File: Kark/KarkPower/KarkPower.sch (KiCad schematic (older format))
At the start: 35 parts, among them J101 CAN_1, J102 CAN_2, J103 CAN_3, J104 CAN_4, J105 CAN_5, J106 CAN_6, J107 CAN_7, J108 CAN_8, J109 CAN_9, J110 JPR_1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

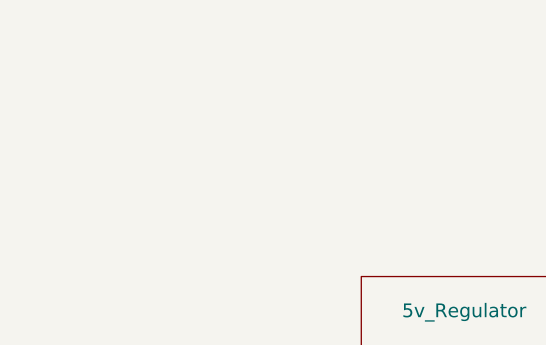
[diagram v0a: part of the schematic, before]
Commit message: PCB Developed Further
Organized and optimized part layout.
(wires not started)
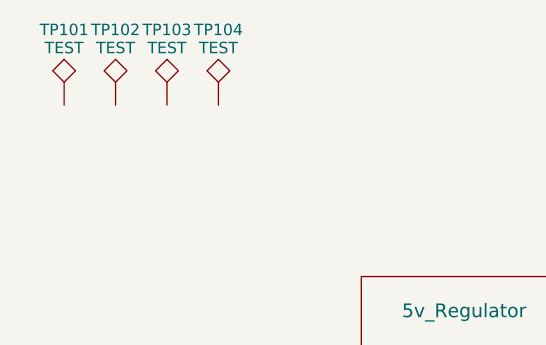
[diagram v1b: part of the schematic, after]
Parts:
- added TP101, TP102, TP103, TP104: TEST, Mounting_Holes:MountingHole_3.2mm_M3_Pad, symbol TEST
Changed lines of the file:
@@
 Wire Wire Line
 	5625 3700 5625 3075
+$Comp
+L TEST TP101
+U 1 1 5A635A3C
+P 1075 2000
+F 0 "TP101" H 1075 2300 50  0000 C BNN
+F 1 "TEST" H 1075 2250 50  0000 C CNN
+F 2 "Mounting_Holes:MountingHole_3.2mm_M3_Pad" H 1075 2000 50  0001 C CNN
+F 3 "" H 1075 2000 50  0001 C CNN
+	1    1075 2000
+	1    0    0    -1
+$EndComp
+$Comp
+L TEST TP102
+U 1 1 5A635CC5
+P 1300 2000
+F 0 "TP102" H 1300 2300 50  0000 C BNN
+F 1 "TEST" H 1300 2250 50  0000 C CNN
+F 2 "Mounting_Holes:MountingHole_3.2mm_M3_Pad" H 1300 2000 50  0001 C CNN
+F 3 "" H 1300 2000 50  0001 C CNN
+	1    1300 2000
+	1    0    0    -1
+$EndComp
+$Comp
+L TEST TP103
+U 1 1 5A635D55
+P 1525 2000
+F 0 "TP103" H 1525 2300 50  0000 C BNN
+F 1 "TEST" H 1525 2250 50  0000 C CNN
+F 2 "Mounting_Holes:MountingHole_3.2mm_M3_Pad" H 1525 2000 50  0001 C CNN
+F 3 "" H 1525 2000 50  0001 C CNN
+	1    1525 2000
+	1    0    0    -1
+$EndComp
+$Comp
+L TEST TP104
+U 1 1 5A635DDC
+P 1750 2000
+F 0 "TP104" H 1750 2300 50  0000 C BNN
+F 1 "TEST" H 1750 2250 50  0000 C CNN
+F 2 "Mounting_Holes:MountingHole_3.2mm_M3_Pad" H 1750 2000 50  0001 C CNN
+F 3 "" H 1750 2000 50  0001 C CNN
+	1    1750 2000
+	1    0    0    -1
+$EndComp
 $EndSCHEMATC

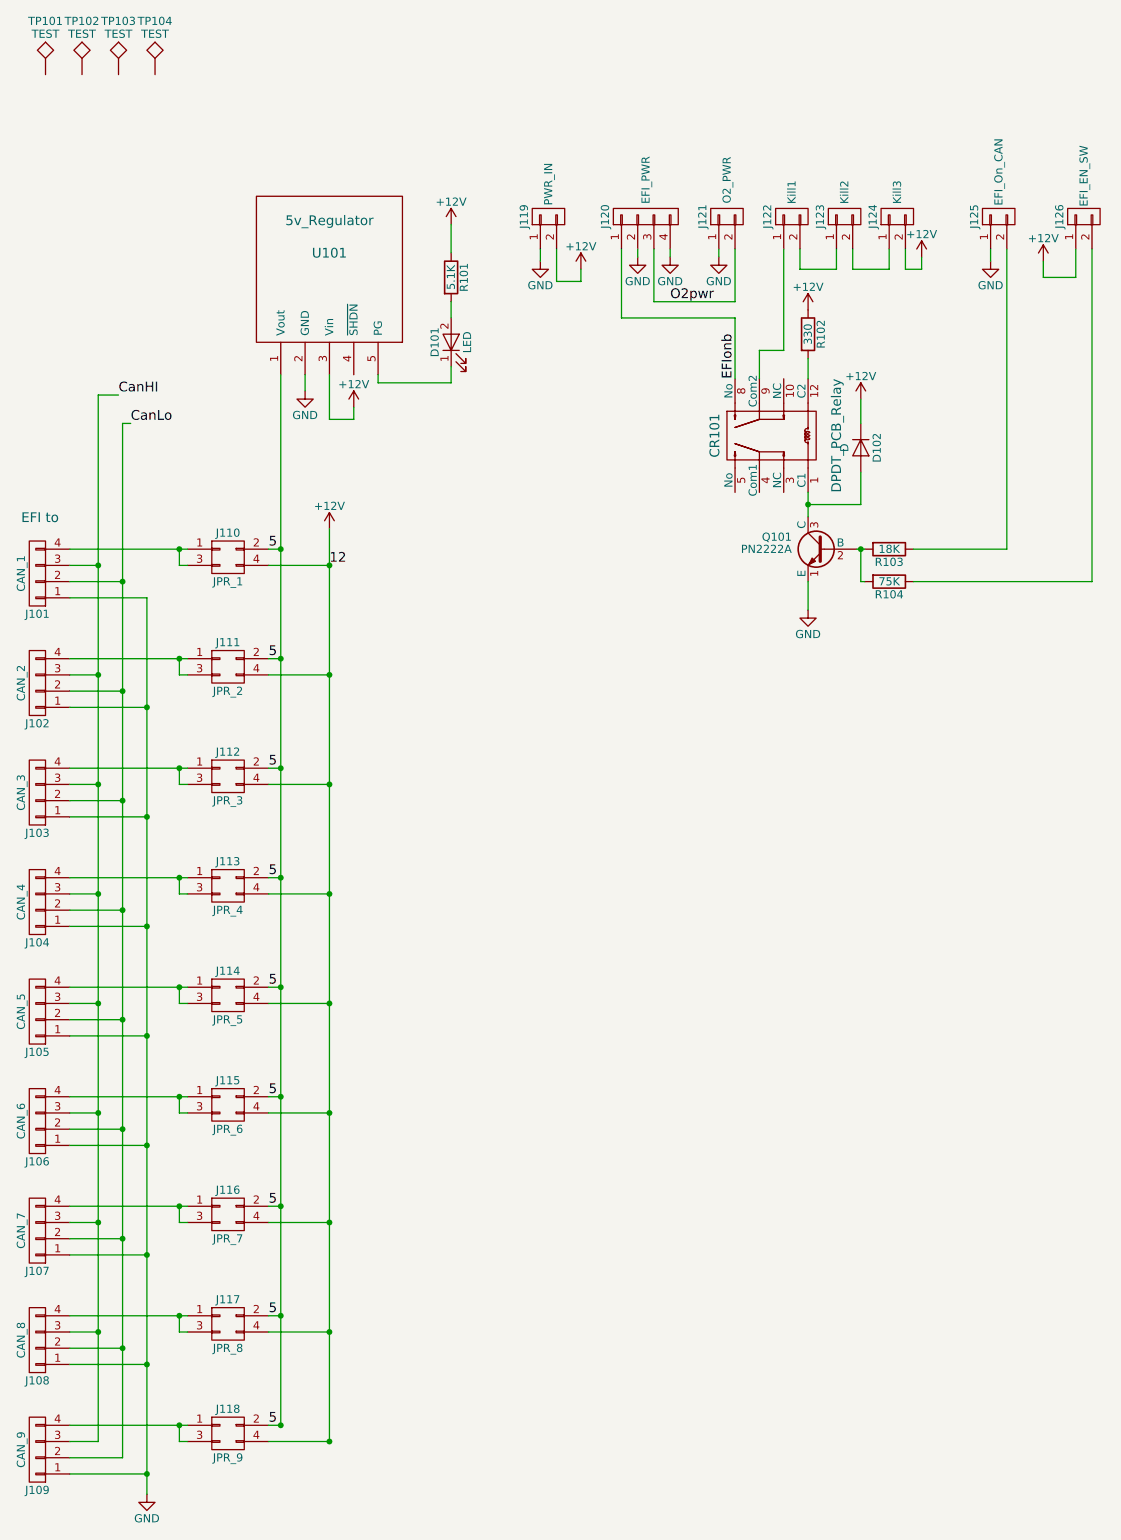
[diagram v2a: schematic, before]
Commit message: Added Starter and Fuel pump
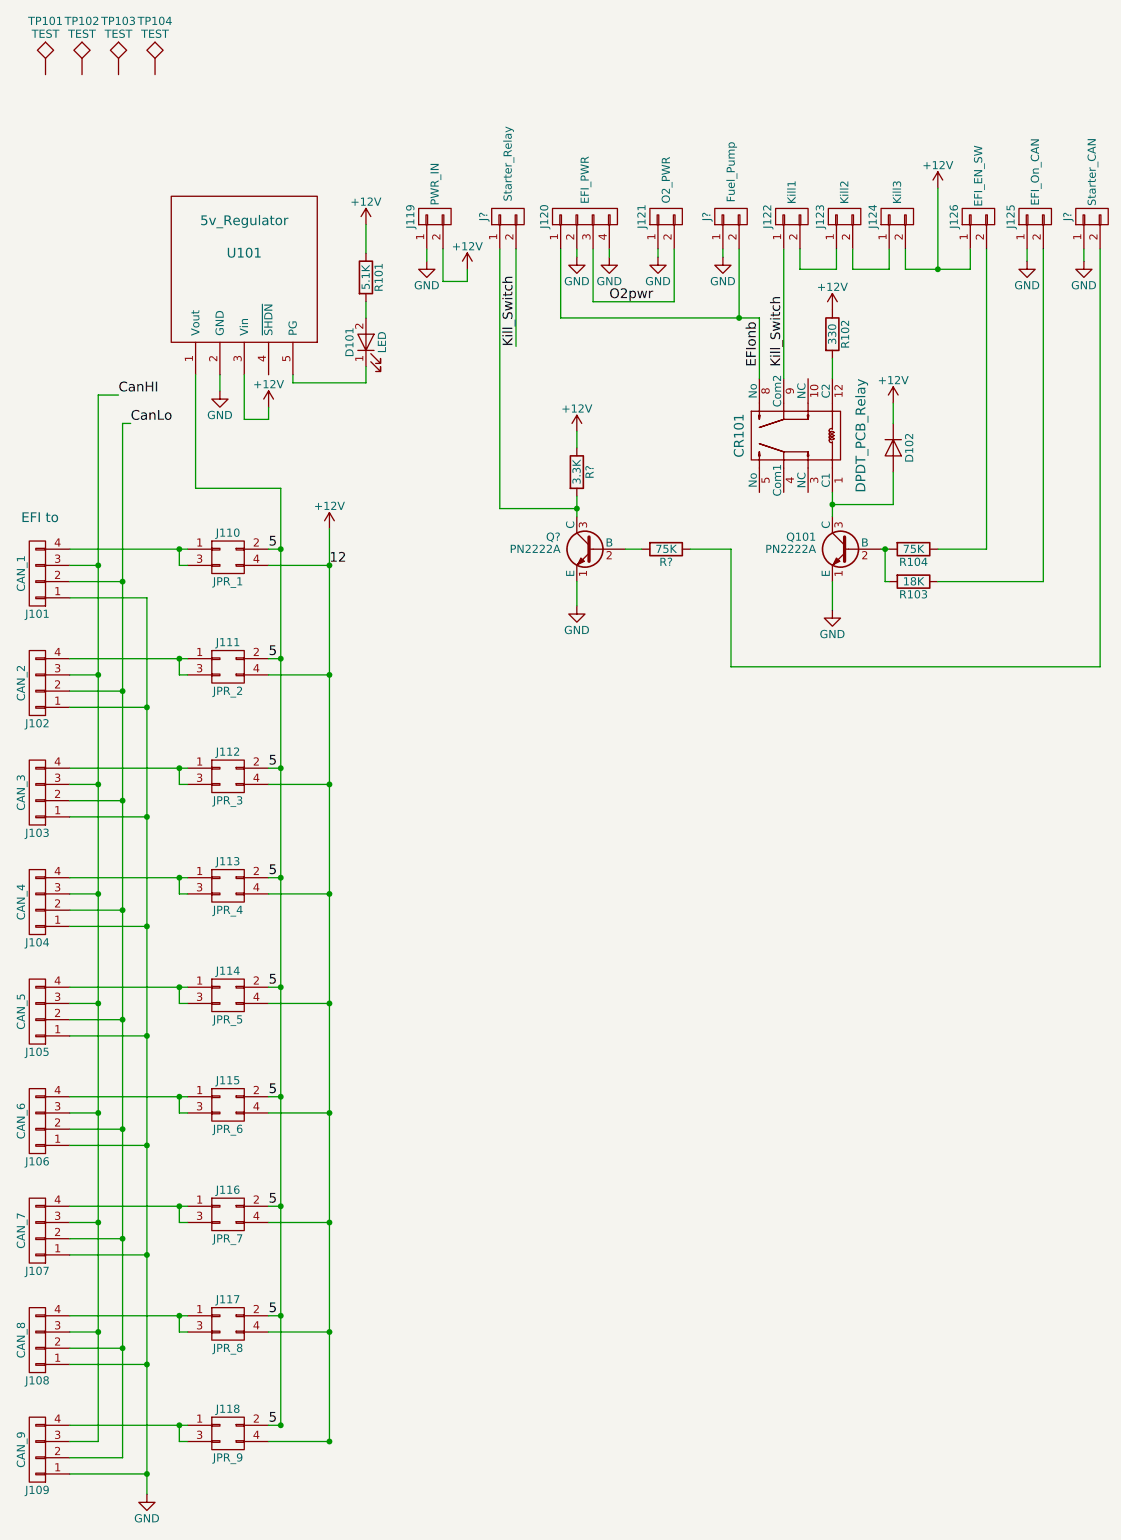
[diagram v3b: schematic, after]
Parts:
- added J?: Fuel_Pump, supermileage_footprints:Molex-UltraFit-2p, symbol CONN_01X02
- added J?: Starter_CAN, supermileage_footprints:Molex-UltraFit-2p, symbol CONN_01X02
- added J?: Starter_Relay, supermileage_footprints:Molex-UltraFit-2p, symbol CONN_01X02
- added Q?: PN2222A, TO_SOT_Packages_THT:TO-92_Inline_Wide, symbol PN2222A
- added R?: 3.3K, symbol R
- added R?: 75K, Resistors_THT:R_Axial_DIN0207_L6.3mm_D2.5mm_P7.62mm_Horizontal, symbol R
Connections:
- net +12V: now also R?.1
- net EFIonb: now also J?.2 (P2)
- net GND: now also J?.1 (P1), J?.1 (P1), Q?.1 (E)
- net Kill_Switch: now reaches CR101.9 (Com2), J122.1 (P1)
- net Kill_Switch: now also J?.2 (P2)
- new net: Q?.2 (B), R?.2
- new net: J?.1 (P1), Q?.3 (C), R?.2
- new net: J?.2 (P2), R?.1
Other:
- moved on the sheet: CR101, D101, D102, J119, J120, J121, J125, J126, Q101, R101, R102, R103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

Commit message: Created can breakout
Added can boards fro sensors and integrated the computer to the can system.
Created the Can powering system.
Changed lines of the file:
@@
 LIBS:supermileage_computers
 LIBS:supermileage_sensors
+LIBS:EllicottDisplay
+LIBS:EllicottInterface
+LIBS:EllicottMicrocontrollers
+LIBS:EllicottMisc
+LIBS:EllicottPower
 LIBS:KarkSchematics-cache
 EELAYER 25 0
@@
 $Descr A4 8268 11693 portrait
 encoding utf-8
-Sheet 4 6
+Sheet 3 9
 Title "Karch Main Power Distribution Hub"
 Date "01/13/18"
@@
 Kill_Switch
 Wire Wire Line
-	1400 3975 1400 5025
-Wire Wire Line
-	1400 5025 1400 5700
-Wire Wire Line
-	1400 5700 1400 6375
-Wire Wire Line
-	1400 6375 1400 7050
-Wire Wire Line
-	1400 7050 1400 7725
-Wire Wire Line
-	1400 7725 1400 8400
-Wire Wire Line
-	1400 8400 1400 9075
-Wire Wire Line
-	1400 9075 1400 9750
-Wire Wire Line
-	1400 9750 1400 10425
-Wire Wire Line
-	1550 4150 1550 5125
-Wire Wire Line
-	1550 5125 1550 5800
-Wire Wire Line
-	1550 5800 1550 6475
-Wire Wire Line
-	1550 6475 1550 7150
-Wire Wire Line
-	1550 7150 1550 7825
-Wire Wire Line
-	1550 7825 1550 8500
-Wire Wire Line
-	1550 8500 1550 9175
-Wire Wire Line
-	1550 9175 1550 9850
-Wire Wire Line
-	1550 9850 1550 10525
+	1400 3975 1400 10425
+Wire Wire Line
+	1550 4150 1550 10525
 Wire Wire Line
 	5725 3075 5725 3200
@@
 	6275 3200 6275 3075
 Wire Wire Line
-	2525 4550 2525 4925
-Wire Wire Line
-	2525 4925 2525 5600
-Wire Wire Line
-	2525 5600 2525 6275
-Wire Wire Line
-	2525 6275 2525 6950
-Wire Wire Line
-	2525 6950 2525 7625
-Wire Wire Line
-	2525 7625 2525 8300
-Wire Wire Line
-	2525 8300 2525 8975
-Wire Wire Line
-	2525 8975 2525 9650
-Wire Wire Line
-	2525 9650 2525 10325
+	2525 4550 2525 10325
 Connection ~ 2525 4925
 Connection ~ 2825 5025
 Wire Wire Line
-	1700 5225 1700 5900
-Wire Wire Line
-	1700 5900 1700 6575
-Wire Wire Line
-	1700 6575 1700 7250
-Wire Wire Line
-	1700 7250 1700 7925
-Wire Wire Line
-	1700 7925 1700 8600
-Wire Wire Line
-	1700 8600 1700 9275
-Wire Wire Line
-	1700 9275 1700 9950
-Wire Wire Line
-	1700 9950 1700 10625
-Wire Wire Line
-	1700 10625 1700 10750
+	1700 5225 1700 10750
 Wire Wire Line
 	1550 4150 1600 4150
@@
 Connection ~ 1400 5025
 Wire Wire Line
-	1225 5600 1900 5600
-Wire Wire Line
-	1900 5600 1950 5600
+	1225 5600 1950 5600
 Wire Wire Line
 	1700 5900 1225 5900
@@
 Connection ~ 2825 5700
 Wire Wire Line
-	1225 4925 1900 4925
-Wire Wire Line
-	1900 4925 1950 4925
+	1225 4925 1950 4925
 Wire Wire Line
 	2525 4925 2450 4925
@@
 Connection ~ 1900 4925
 Wire Wire Line
-	1225 6275 1900 6275
-Wire Wire Line
-	1900 6275 1950 6275
+	1225 6275 1950 6275
 Wire Wire Line
 	1700 6575 1225 6575
@@
 Connection ~ 2825 6375
 Wire Wire Line
-	1225 6950 1900 6950
-Wire Wire Line
-	1900 6950 1950 6950
+	1225 6950 1950 6950
 Wire Wire Line
 	1700 7250 1225 7250
@@
 Connection ~ 2825 7050
 Wire Wire Line
-	1225 7625 1900 7625
-Wire Wire Line
-	1900 7625 1950 7625
+	1225 7625 1950 7625
 Wire Wire Line
 	1700 7925 1225 7925
@@
 Connection ~ 2525 7625
 Wire Wire Line
-	1225 8300 1900 8300
-Wire Wire Line
-	1900 8300 1950 8300
+	1225 8300 1950 8300
 Wire Wire Line
 	1700 8600 1225 8600
@@
 Connection ~ 2825 8400
 Wire Wire Line
-	1225 8975 1900 8975
-Wire Wire Line
-	1900 8975 1950 8975
+	1225 8975 1950 8975
 Wire Wire Line
 	1700 9275 1225 9275
@@
 Connection ~ 2825 9075
 Wire Wire Line
-	1225 9650 1900 9650
-Wire Wire Line
-	1900 9650 1950 9650
+	1225 9650 1950 9650
 Wire Wire Line
 	1700 9950 1225 9950
@@
 Connection ~ 2825 9750
 Wire Wire Line
-	1225 10325 1900 10325
-Wire Wire Line
-	1900 10325 1950 10325
+	1225 10325 1950 10325
 Wire Wire Line
 	1700 10625 1225 10625
@@
 Connection ~ 2825 10425
 Wire Wire Line
-	6225 4925 6250 4925
-Wire Wire Line
-	6250 4925 6275 4925
+	6225 4925 6275 4925
 Wire Wire Line
 	6250 4925 6250 5125
@@
 Connection ~ 6250 4925
 Wire Wire Line
-	5925 4575 5925 4650
-Wire Wire Line
-	5925 4650 5925 4725
+	5925 4575 5925 4725
 Wire Wire Line
 	4250 3075 4250 3500
 Wire Wire Line
-	2825 4800 2825 5025
-Wire Wire Line
-	2825 5025 2825 5700
-Wire Wire Line
-	2825 5700 2825 6375
-Wire Wire Line
-	2825 6375 2825 7050
-Wire Wire Line
-	2825 7050 2825 7725
-Wire Wire Line
-	2825 7725 2825 8400
-Wire Wire Line
-	2825 8400 2825 9075
-Wire Wire Line
-	2825 9075 2825 9750
-Wire Wire Line
-	2825 9750 2825 10425
+	2825 4800 2825 10425
 Connection ~ 2825 7725
 Wire Wire Line
@@
 	6375 3075 6375 3200
 Wire Wire Line
-	6375 3200 6575 3200
-Wire Wire Line
-	6575 3200 6775 3200
+	6375 3200 6775 3200
 Wire Wire Line
 	6575 3200 6575 2700
@@
 	4450 3400 4450 3075
 Wire Wire Line
-	4250 3500 5350 3500
-Wire Wire Line
-	5350 3500 5475 3500
+	4250 3500 5475 3500
 Wire Wire Line
 	7225 5125 7225 3075
@@
 	4350 5275 4350 5125
 Wire Wire Line
-	4350 4725 4350 4675
-Wire Wire Line
-	4350 4675 4350 4600
+	4350 4600 4350 4725
 $Comp
 L +12V #PWR?
